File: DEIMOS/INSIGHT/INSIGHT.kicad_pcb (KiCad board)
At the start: 4 copper layers, 76.8 x 38.1 mm, 76 parts, among them J1 Batt, J2 SMA-J-P-GF-RA-SM1, J3 USB_C_Receptacle_USB2.0_16P, J4 Boot, J5 GND, SW3 SW_SPDT, U1 LSM6DS3, U2 MPL3115A2, U3 W25Q128JVSIQ, U4 BNO085, U5 RP2040, U6 Adafruit GPS, U7 MPM3610GQV-Z, U8 RFM95W-915S2, Y1 ABM8-272-T3, Y2 ABS07-32.768KHZ-1-T

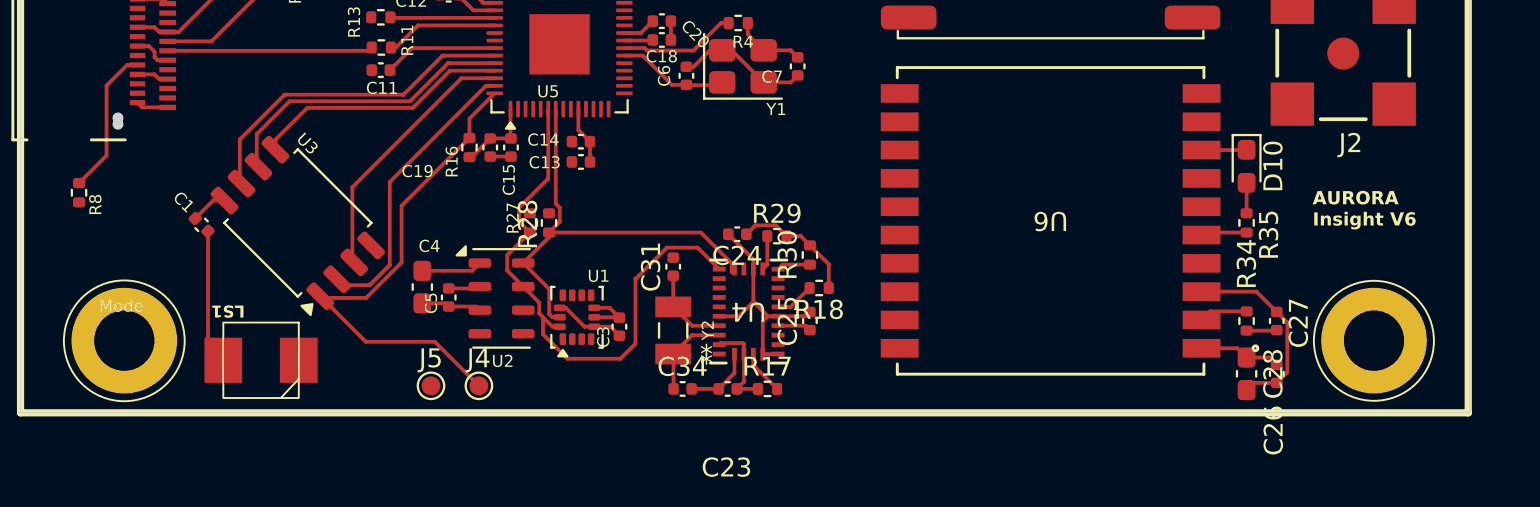
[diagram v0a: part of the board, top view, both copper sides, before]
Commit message: 3d models added
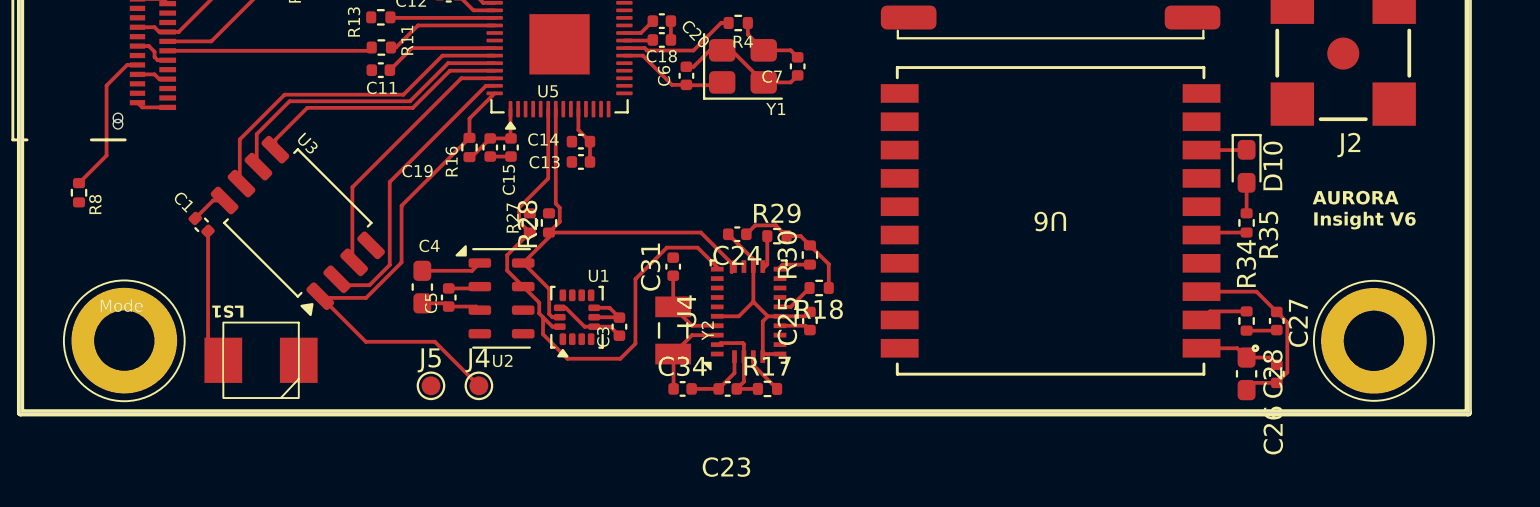
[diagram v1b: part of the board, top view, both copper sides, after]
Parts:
- U4: footprint footprints:LGA-28_CEV -> Package_LGA:LGA-28_5.2x3.8mm_P0.5mm
- turned U4 to 90 degrees
